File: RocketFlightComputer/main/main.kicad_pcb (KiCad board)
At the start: 2 copper layers, 62 x 62 mm, 0 parts

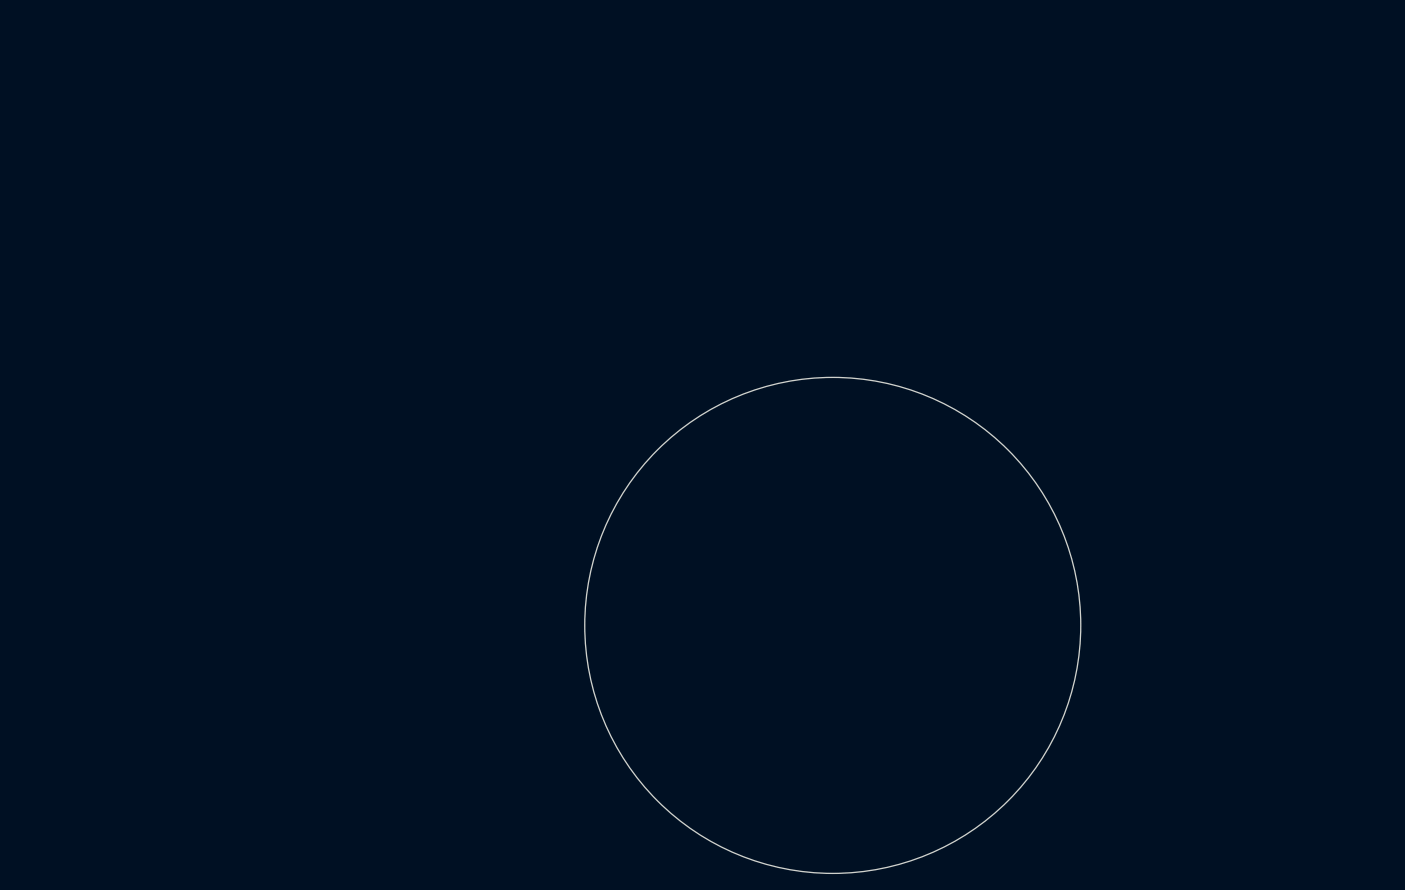
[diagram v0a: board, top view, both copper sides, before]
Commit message: CID documentation and started the PCB editor process
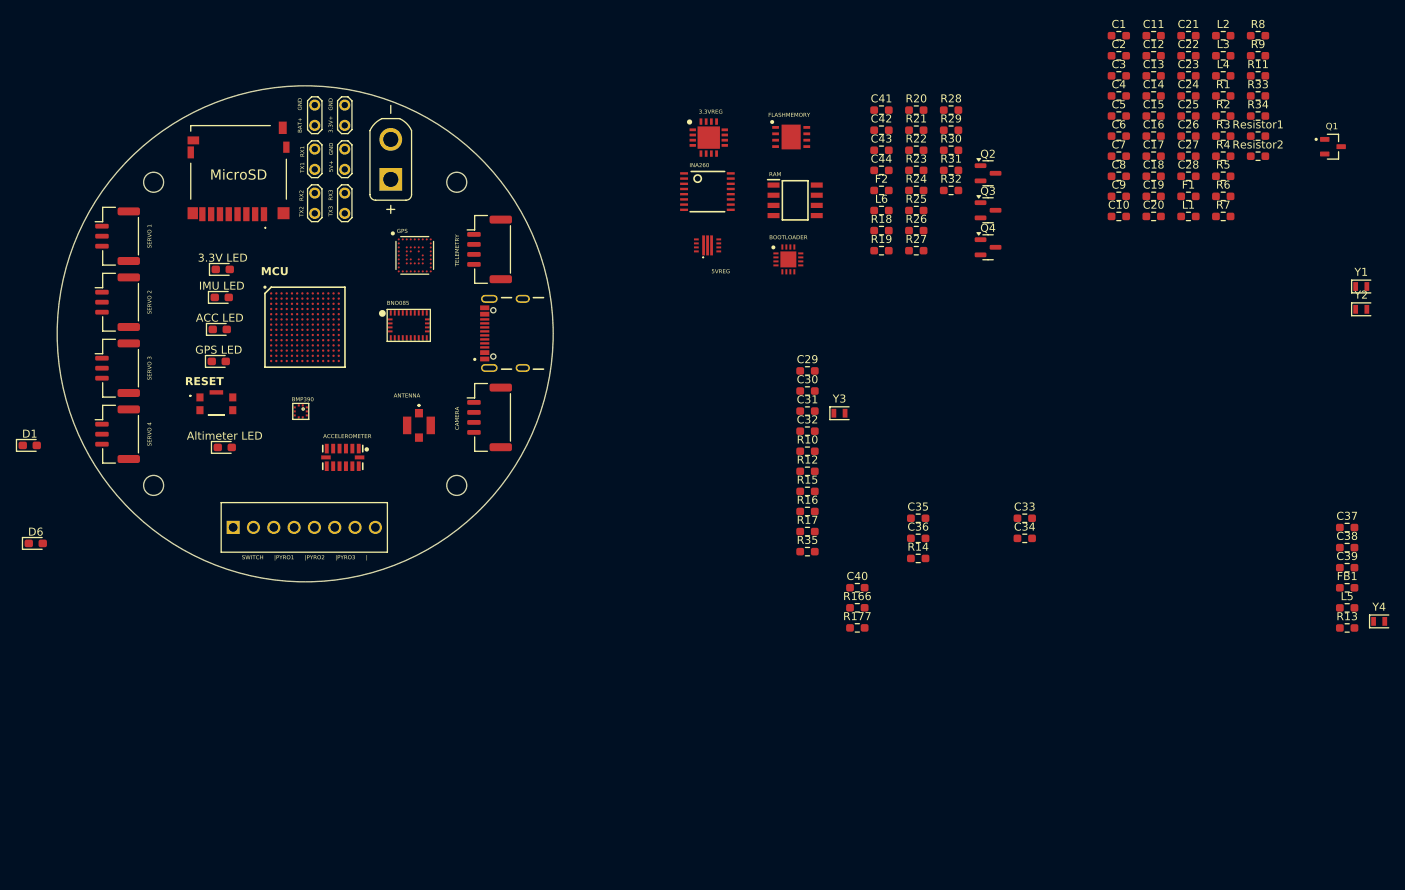
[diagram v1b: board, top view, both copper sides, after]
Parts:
- added 3.3V LED: 3.3V LED, LED_SMD:LED_0603_1608Metric_Pad1.05x0.95mm_HandSolder, F.Cu at (103.2, 89.2)
- added 3.3V+   GND: TestPoint_2Pole, TestPoint:TestPoint_2Pads_Pitch2.54mm_Drill0.8mm, F.Cu at (118.5, 71.2)
- added 3.3VREG: TPS62111RSAR, footprint:TPS62111RSAR, F.Cu at (164.0, 72.8)
- added 5V+   GND: TestPoint_2Pole, TestPoint:TestPoint_2Pads_Pitch2.54mm_Drill0.8mm, F.Cu at (118.5, 76.8)
- added 5VREG: TPS621361RGXT, footprint:TPS621361RGXT, F.Cu at (163.8, 86.2)
- added ACC LED: 200G ACC LED, LED_SMD:LED_0603_1608Metric_Pad1.05x0.95mm_HandSolder, F.Cu at (102.9, 96.8)
- added ACCELEROMETER: ADXL375, ADXL375:LGA14, F.Cu at (118.2, 112.8)
- added ANTENNA: CONMHF1-SMD-G-T, footprint:CONMHF1SMDGT, F.Cu at (127.8, 108.8)
- added Altimeter LED: Altimeter LED, LED_SMD:LED_0603_1608Metric_Pad1.05x0.95mm_HandSolder, F.Cu at (103.5, 111.5)
- added BAT+    GND: TestPoint_2Pole, TestPoint:TestPoint_2Pads_Pitch2.54mm_Drill0.8mm, F.Cu at (114.8, 71.2)
- added BMP390: BMP390, BMP390:BMP388, F.Cu at (113.0, 107.0)
- added BOOTLOADER: MKL02Z32VFG4, footprint:QFN50P300X300X65-17N-D, F.Cu at (173.9, 88.0)
- added BatteryConnector1: XT30UPB-M, XT30:AMASS_XT30UPB-M, F.Cu at (124.2, 75.5)
- added C1: 10uF, Resistor_SMD:R_0603_1608Metric_Pad0.98x0.95mm_HandSolder, F.Cu at (215.3, 60.0)
- added C10: 20pF, Resistor_SMD:R_0603_1608Metric_Pad0.98x0.95mm_HandSolder, F.Cu at (215.3, 82.6)
- added C11: 20pF, Resistor_SMD:R_0603_1608Metric_Pad0.98x0.95mm_HandSolder, F.Cu at (219.6, 60.0)
- added C12: 10uF, Resistor_SMD:R_0603_1608Metric_Pad0.98x0.95mm_HandSolder, F.Cu at (219.6, 62.5)
- added C13: 0.22uF, Resistor_SMD:R_0603_1608Metric_Pad0.98x0.95mm_HandSolder, F.Cu at (219.6, 65.1)
- added C14: 0.22uF, Resistor_SMD:R_0603_1608Metric_Pad0.98x0.95mm_HandSolder, F.Cu at (219.6, 67.6)
- added C15: 4.7uF, Resistor_SMD:R_0603_1608Metric_Pad0.98x0.95mm_HandSolder, F.Cu at (219.6, 70.1)
- added C16: 4.7uF, Resistor_SMD:R_0603_1608Metric_Pad0.98x0.95mm_HandSolder, F.Cu at (219.6, 72.6)
- added C17: 4.7uF, Resistor_SMD:R_0603_1608Metric_Pad0.98x0.95mm_HandSolder, F.Cu at (219.6, 75.1)
- added C18: 0.22uF, Resistor_SMD:R_0603_1608Metric_Pad0.98x0.95mm_HandSolder, F.Cu at (219.6, 77.6)
- added C19: 0.22uF, Resistor_SMD:R_0603_1608Metric_Pad0.98x0.95mm_HandSolder, F.Cu at (219.6, 80.1)
- added C2: 22uF, Resistor_SMD:R_0603_1608Metric_Pad0.98x0.95mm_HandSolder, F.Cu at (215.3, 62.5)
- added C20: 0.22uF, Resistor_SMD:R_0603_1608Metric_Pad0.98x0.95mm_HandSolder, F.Cu at (219.6, 82.6)
- added C21: 0.22uF, Resistor_SMD:R_0603_1608Metric_Pad0.98x0.95mm_HandSolder, F.Cu at (224.0, 60.0)
- added C22: 0.22uF, Resistor_SMD:R_0603_1608Metric_Pad0.98x0.95mm_HandSolder, F.Cu at (224.0, 62.5)
- added C23: 12pF, Resistor_SMD:R_0603_1608Metric_Pad0.98x0.95mm_HandSolder, F.Cu at (224.0, 65.1)
- added C24: 12pF, Resistor_SMD:R_0603_1608Metric_Pad0.98x0.95mm_HandSolder, F.Cu at (224.0, 67.6)
- added C25: 10nF, Resistor_SMD:R_0603_1608Metric_Pad0.98x0.95mm_HandSolder, F.Cu at (224.0, 70.1)
- added C26: 0.22uF, Resistor_SMD:R_0603_1608Metric_Pad0.98x0.95mm_HandSolder, F.Cu at (224.0, 72.6)
- added C27: 4.7uF, Resistor_SMD:R_0603_1608Metric_Pad0.98x0.95mm_HandSolder, F.Cu at (224.0, 75.1)
- added C28: 10uF, Resistor_SMD:R_0603_1608Metric_Pad0.98x0.95mm_HandSolder, F.Cu at (224.0, 77.6)
- added C29: 0.1uF, Resistor_SMD:R_0603_1608Metric_Pad0.98x0.95mm_HandSolder, F.Cu at (176.3, 101.9)
- added C3: 1uF, Resistor_SMD:R_0603_1608Metric_Pad0.98x0.95mm_HandSolder, F.Cu at (215.3, 65.1)
- added C30: 0.1uF, Resistor_SMD:R_0603_1608Metric_Pad0.98x0.95mm_HandSolder, F.Cu at (176.3, 104.5)
- added C31: 22pF, Resistor_SMD:R_0603_1608Metric_Pad0.98x0.95mm_HandSolder, F.Cu at (176.3, 107.0)
- added C32: 22pF, Resistor_SMD:R_0603_1608Metric_Pad0.98x0.95mm_HandSolder, F.Cu at (176.3, 109.5)
- added C33: 0.1uF, Resistor_SMD:R_0603_1608Metric_Pad0.98x0.95mm_HandSolder, F.Cu at (203.5, 120.4)
- added C34: 0.1uF, Resistor_SMD:R_0603_1608Metric_Pad0.98x0.95mm_HandSolder, F.Cu at (203.5, 122.9)
- added C35: 1uF, Resistor_SMD:R_0603_1608Metric_Pad0.98x0.95mm_HandSolder, F.Cu at (190.2, 120.4)
- added C36: 0.1uF, Resistor_SMD:R_0603_1608Metric_Pad0.98x0.95mm_HandSolder, F.Cu at (190.2, 122.9)
- added C37: 47PF-0603-50V-5%, Resistor_SMD:R_0603_1608Metric_Pad0.98x0.95mm_HandSolder, F.Cu at (243.8, 121.5)
- added C38: 4.7UF, Resistor_SMD:R_0603_1608Metric_Pad0.98x0.95mm_HandSolder, F.Cu at (243.8, 124.0)
- added C39: 0.1UF, Resistor_SMD:R_0603_1608Metric_Pad0.98x0.95mm_HandSolder, F.Cu at (243.8, 126.5)
- added C4: 0.22uF, Resistor_SMD:R_0603_1608Metric_Pad0.98x0.95mm_HandSolder, F.Cu at (215.3, 67.6)
- added C40: 1uF, Resistor_SMD:R_0603_1608Metric_Pad0.98x0.95mm_HandSolder, F.Cu at (182.6, 129.0)
- added C41: 10uF, Resistor_SMD:R_0603_1608Metric_Pad0.98x0.95mm_HandSolder, F.Cu at (185.6, 69.3)
- added C42: 22uF, Resistor_SMD:R_0603_1608Metric_Pad0.98x0.95mm_HandSolder, F.Cu at (185.6, 71.8)
- added C43: 22uF, Resistor_SMD:R_0603_1608Metric_Pad0.98x0.95mm_HandSolder, F.Cu at (185.6, 74.4)
- added C44: 3.3nF, Resistor_SMD:R_0603_1608Metric_Pad0.98x0.95mm_HandSolder, F.Cu at (185.6, 76.9)
- added C5: 0.22uF, Resistor_SMD:R_0603_1608Metric_Pad0.98x0.95mm_HandSolder, F.Cu at (215.3, 70.1)
- added C6: 0.22uF, Resistor_SMD:R_0603_1608Metric_Pad0.98x0.95mm_HandSolder, F.Cu at (215.3, 72.6)
- added C7: 2.2uF, Resistor_SMD:R_0603_1608Metric_Pad0.98x0.95mm_HandSolder, F.Cu at (215.3, 75.1)
- added C8: 10nF, Resistor_SMD:R_0603_1608Metric_Pad0.98x0.95mm_HandSolder, F.Cu at (215.3, 77.6)
- added C9: 4.7uF, Resistor_SMD:R_0603_1608Metric_Pad0.98x0.95mm_HandSolder, F.Cu at (215.3, 80.1)
- added CAMERA: S4B-PH-K-S_LF__SN_, Connector_JST:JST_GH_BM04B-GHS-TBT_1x04-1MP_P1.25mm_Vertical, F.Cu at (136.6, 107.8)
- added D1: LED, LED_SMD:LED_0603_1608Metric_Pad1.05x0.95mm_HandSolder, F.Cu at (79.1, 111.2)
- added D6: Misc LED, LED_SMD:LED_0603_1608Metric_Pad1.05x0.95mm_HandSolder, F.Cu at (79.9, 123.5)
- added F1: 1A, Resistor_SMD:R_0603_1608Metric_Pad0.98x0.95mm_HandSolder, F.Cu at (224.0, 80.1)
- added F2: 5A, Resistor_SMD:R_0603_1608Metric_Pad0.98x0.95mm_HandSolder, F.Cu at (185.6, 79.4)
- added FB1: 120ohm, Resistor_SMD:R_0603_1608Metric_Pad0.98x0.95mm_HandSolder, F.Cu at (243.8, 129.1)
- added FLASHMEMORY: W25Q64JVXGIM_TR, footprint:SON80P400X400X50-9N, F.Cu at (174.3, 72.7)
- added GPS LED: GPS LED, LED_SMD:LED_0603_1608Metric_Pad1.05x0.95mm_HandSolder, F.Cu at (102.8, 100.8)
- added IMU LED: IMU LED, LED_SMD:LED_0603_1608Metric_Pad1.05x0.95mm_HandSolder, F.Cu at (103.1, 92.8)
- added INA260: INA260, INA260:TSSOP16, F.Cu at (163.8, 79.5)
- added L1: 120, Resistor_SMD:R_0603_1608Metric_Pad0.98x0.95mm_HandSolder, F.Cu at (224.0, 82.6)
- added L2: 6.8uH, Resistor_SMD:R_0603_1608Metric_Pad0.98x0.95mm_HandSolder, F.Cu at (228.3, 60.0)
- added L3: 120, Resistor_SMD:R_0603_1608Metric_Pad0.98x0.95mm_HandSolder, F.Cu at (228.3, 62.5)
- added L4: 4.7uH, Resistor_SMD:R_0603_1608Metric_Pad0.98x0.95mm_HandSolder, F.Cu at (228.3, 65.1)
- added L5: 2.2μ, Resistor_SMD:R_0603_1608Metric_Pad0.98x0.95mm_HandSolder, F.Cu at (243.8, 131.6)
- added L6: 1.5uH, Resistor_SMD:R_0603_1608Metric_Pad0.98x0.95mm_HandSolder, F.Cu at (185.6, 81.9)
- added MCU: MIMXRT1062DVL6B, footprint:BGA196C65P14X14_1000X1000X152, F.Cu at (113.5, 96.5)
- added MicroSD: DM3D-SF, DM3DSF:DM3DSF, F.Cu at (105.2, 77.0)
- added Q1: DMG2305UX, footprint:DMG2305UX, F.Cu at (242.0, 73.9)
- added Q2: SI2302, Package_TO_SOT_SMD:SOT-23, F.Cu at (198.9, 77.2)
- added Q3: SI2302, Package_TO_SOT_SMD:SOT-23, F.Cu at (198.9, 81.9)
- added Q4: SI2302, Package_TO_SOT_SMD:SOT-23, F.Cu at (198.9, 86.5)
- added R1: 1M, Resistor_SMD:R_0603_1608Metric_Pad0.98x0.95mm_HandSolder, F.Cu at (228.3, 67.6)
- added R10: 10k, Resistor_SMD:R_0603_1608Metric_Pad0.98x0.95mm_HandSolder, F.Cu at (176.3, 112.0)
- added R11: 4.7k, Resistor_SMD:R_0603_1608Metric_Pad0.98x0.95mm_HandSolder, F.Cu at (232.7, 65.1)
- added R12: 10k, Resistor_SMD:R_0603_1608Metric_Pad0.98x0.95mm_HandSolder, F.Cu at (176.3, 114.5)
- added R13: 10OHM-0603-1/10W-1%, Resistor_SMD:R_0603_1608Metric_Pad0.98x0.95mm_HandSolder, F.Cu at (243.8, 134.1)
- added R14: 10k, Resistor_SMD:R_0603_1608Metric_Pad0.98x0.95mm_HandSolder, F.Cu at (190.2, 125.4)
- added R15: 4.7k, Resistor_SMD:R_0603_1608Metric_Pad0.98x0.95mm_HandSolder, F.Cu at (176.3, 117.0)
- added R16: 4.7k, Resistor_SMD:R_0603_1608Metric_Pad0.98x0.95mm_HandSolder, F.Cu at (176.3, 119.5)
- added R166: 10K, Resistor_SMD:R_0603_1608Metric_Pad0.98x0.95mm_HandSolder, F.Cu at (182.6, 131.6)
- added R17: 4.7k, Resistor_SMD:R_0603_1608Metric_Pad0.98x0.95mm_HandSolder, F.Cu at (176.3, 122.0)
- added R177: 10K, Resistor_SMD:R_0603_1608Metric_Pad0.98x0.95mm_HandSolder, F.Cu at (182.6, 134.1)
- added R18: 10k, Resistor_SMD:R_0603_1608Metric_Pad0.98x0.95mm_HandSolder, F.Cu at (185.6, 84.4)
- added R19: 4, Resistor_SMD:R_0603_1608Metric_Pad0.98x0.95mm_HandSolder, F.Cu at (185.6, 86.9)
- added R2: 470, Resistor_SMD:R_0603_1608Metric_Pad0.98x0.95mm_HandSolder, F.Cu at (228.3, 70.1)
- added R20: 7k, Resistor_SMD:R_0603_1608Metric_Pad0.98x0.95mm_HandSolder, F.Cu at (189.9, 69.3)
- added R21: 10k, Resistor_SMD:R_0603_1608Metric_Pad0.98x0.95mm_HandSolder, F.Cu at (189.9, 71.8)
- added R22: 470k, Resistor_SMD:R_0603_1608Metric_Pad0.98x0.95mm_HandSolder, F.Cu at (189.9, 74.4)
- added R23: 10k, Resistor_SMD:R_0603_1608Metric_Pad0.98x0.95mm_HandSolder, F.Cu at (189.9, 76.9)
- added R24: 4, Resistor_SMD:R_0603_1608Metric_Pad0.98x0.95mm_HandSolder, F.Cu at (189.9, 79.4)
- added R25: 510k, Resistor_SMD:R_0603_1608Metric_Pad0.98x0.95mm_HandSolder, F.Cu at (189.9, 81.9)
- added R26: 82k, Resistor_SMD:R_0603_1608Metric_Pad0.98x0.95mm_HandSolder, F.Cu at (189.9, 84.4)
- added R27: 7k, Resistor_SMD:R_0603_1608Metric_Pad0.98x0.95mm_HandSolder, F.Cu at (189.9, 86.9)
- added R28: 10k, Resistor_SMD:R_0603_1608Metric_Pad0.98x0.95mm_HandSolder, F.Cu at (194.3, 69.3)
- added R29: 10k, Resistor_SMD:R_0603_1608Metric_Pad0.98x0.95mm_HandSolder, F.Cu at (194.3, 71.8)
- added R3: 470, Resistor_SMD:R_0603_1608Metric_Pad0.98x0.95mm_HandSolder, F.Cu at (228.3, 72.6)
- added R30: 4, Resistor_SMD:R_0603_1608Metric_Pad0.98x0.95mm_HandSolder, F.Cu at (194.3, 74.4)
- added R31: 7k, Resistor_SMD:R_0603_1608Metric_Pad0.98x0.95mm_HandSolder, F.Cu at (194.3, 76.9)
- added R32: 10k, Resistor_SMD:R_0603_1608Metric_Pad0.98x0.95mm_HandSolder, F.Cu at (194.3, 79.4)
- added R33: 470, Resistor_SMD:R_0603_1608Metric_Pad0.98x0.95mm_HandSolder, F.Cu at (232.7, 67.6)
- added R34: 4.7k, Resistor_SMD:R_0603_1608Metric_Pad0.98x0.95mm_HandSolder, F.Cu at (232.7, 70.1)
- added R35: 10k, Resistor_SMD:R_0603_1608Metric_Pad0.98x0.95mm_HandSolder, F.Cu at (176.3, 124.5)
- added R4: 2.2M, Resistor_SMD:R_0603_1608Metric_Pad0.98x0.95mm_HandSolder, F.Cu at (228.3, 75.1)
- added R5: 470, Resistor_SMD:R_0603_1608Metric_Pad0.98x0.95mm_HandSolder, F.Cu at (228.3, 77.6)
- added R6: 470, Resistor_SMD:R_0603_1608Metric_Pad0.98x0.95mm_HandSolder, F.Cu at (228.3, 80.1)
- added R7: 470, Resistor_SMD:R_0603_1608Metric_Pad0.98x0.95mm_HandSolder, F.Cu at (228.3, 82.6)
- added R8: 470, Resistor_SMD:R_0603_1608Metric_Pad0.98x0.95mm_HandSolder, F.Cu at (232.7, 60.0)
- added R9: 100k, Resistor_SMD:R_0603_1608Metric_Pad0.98x0.95mm_HandSolder, F.Cu at (232.7, 62.5)
- added RAM: APS6404L-3SQR-SN, footprint:APS6404L, F.Cu at (174.8, 80.6)
- added REF**: MountingHole_2.5mm, MountingHole:MountingHole_2.5mm, F.Cu at (94.6, 116.2)
- added REF**: MountingHole_2.5mm, MountingHole:MountingHole_2.5mm, F.Cu at (132.5, 116.2)
- added REF**: MountingHole_2.5mm, MountingHole:MountingHole_2.5mm, F.Cu at (132.5, 78.4)
- added REF**: MountingHole_2.5mm, MountingHole:MountingHole_2.5mm, F.Cu at (94.6, 78.4)
- added RESET: KMR241GLFS, footprint:KMR421GULCLFS, F.Cu at (102.5, 106.0)
- added Resistor1: 5.1k, Resistor_SMD:R_0603_1608Metric_Pad0.98x0.95mm_HandSolder, F.Cu at (232.7, 72.6)
- added Resistor2: 5.1k, Resistor_SMD:R_0603_1608Metric_Pad0.98x0.95mm_HandSolder, F.Cu at (232.7, 75.1)
- added SERVO 1: ~, Connector_JST:JST_GH_BM03B-GHS-TBT_1x03-1MP_P1.25mm_Vertical, F.Cu at (90.1, 85.1)
- added SERVO 2: ~, Connector_JST:JST_GH_BM03B-GHS-TBT_1x03-1MP_P1.25mm_Vertical, F.Cu at (90.1, 93.3)
- added SERVO 3: ~, Connector_JST:JST_GH_BM03B-GHS-TBT_1x03-1MP_P1.25mm_Vertical, F.Cu at (90.1, 101.6)
- added SERVO 4: ~, Connector_JST:JST_GH_BM03B-GHS-TBT_1x03-1MP_P1.25mm_Vertical, F.Cu at (90.1, 109.8)
- added SWITCH      |PYRO1      |PYRO2      |PYRO3      |: 1725711, footprint:1725711, F.Cu at (104.5, 121.5)
- added TELEMETRY: S4B-PH-K-S_LF__SN_, Connector_JST:JST_GH_BM04B-GHS-TBT_1x04-1MP_P1.25mm_Vertical, F.Cu at (136.6, 86.8)
- added TX1   RX1: TestPoint_2Pole, TestPoint:TestPoint_2Pads_Pitch2.54mm_Drill0.8mm, F.Cu at (114.8, 76.8)
- added TX2   RX2: TestPoint_2Pole, TestPoint:TestPoint_2Pads_Pitch2.54mm_Drill0.8mm, F.Cu at (114.8, 82.2)
- added TX3   RX3: TestPoint_2Pole, TestPoint:TestPoint_2Pads_Pitch2.54mm_Drill0.8mm, F.Cu at (118.5, 82.2)
- added U1: BNO085, BNO08x:BNO080, F.Cu at (126.5, 96.2)
- added U3: GPS, ZOE-M8Q:UBLOX_ZOE_M8-0-10, F.Cu at (127.2, 87.5)
- added USBc1: USBc, footprint:GCT_USB4105-GF-A, F.Cu at (140.8, 97.2)
- added Y1: 32.768kHz, Crystal:Crystal_SMD_2012-2Pin_2.0x1.2mm, F.Cu at (245.6, 91.4)
- added Y2: 24MHz, Crystal:Crystal_SMD_2012-2Pin_2.0x1.2mm, F.Cu at (245.6, 94.2)
- added Y3: 32.768kHz, Crystal:Crystal_SMD_2012-2Pin_2.0x1.2mm, F.Cu at (180.3, 107.2)
- added Y4: 32.768kHz, Crystal:Crystal_SMD_2012-2Pin_2.0x1.2mm, F.Cu at (247.8, 133.2)
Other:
- copper layers 2 -> 4

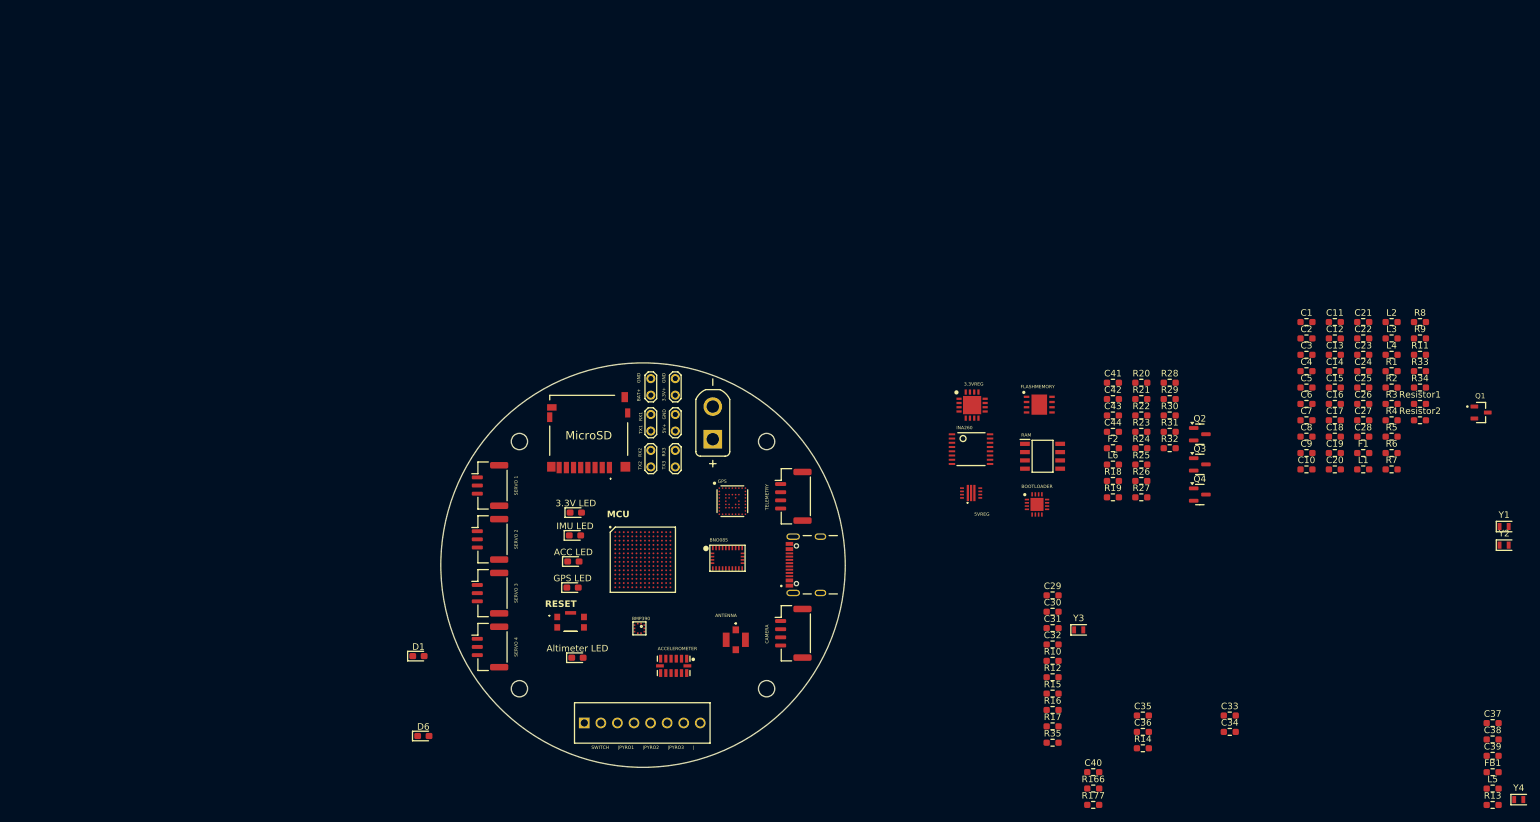
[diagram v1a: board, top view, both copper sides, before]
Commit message: Layout of PCB mostly done
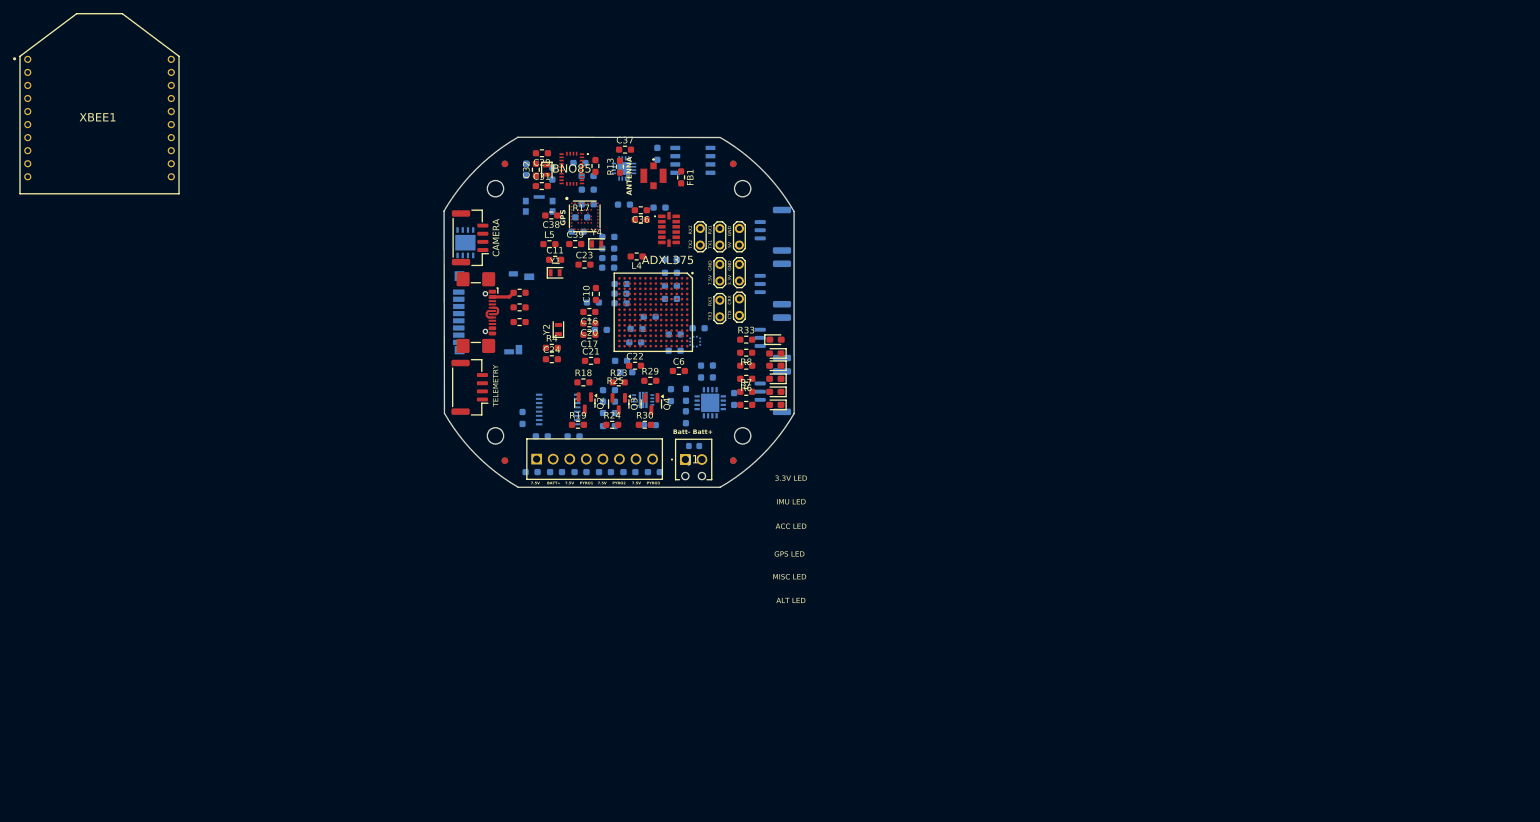
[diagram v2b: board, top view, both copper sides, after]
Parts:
- removed ACCELEROMETER: ADXL375, ADXL375:LGA14
- removed BatteryConnector1: XT30UPB-M, XT30:AMASS_XT30UPB-M
- removed F1: 1A, Resistor_SMD:R_0603_1608Metric_Pad0.98x0.95mm_HandSolder
- removed Q1: DMG2305UX, footprint:DMG2305UX
- removed Resistor1, Resistor2: 5.1k, Resistor_SMD:R_0603_1608Metric_Pad0.98x0.95mm_HandSolder
- removed U1: BNO085, BNO08x:BNO080
- removed USBc1: USBc, footprint:GCT_USB4105-GF-A
- added ADXL375: ACC, footprint:ADXL375BCCZRL, F.Cu at (117.5, 45.8)
- added BNO85: IMU, footprint:BNO085, F.Cu at (102.6, 36.5)
- added FID1: Fiducial, Fiducial:Fiducial_1mm_Mask2mm, F.Cu at (92.4, 35.8)
- added FID2: Fiducial, Fiducial:Fiducial_1mm_Mask2mm, F.Cu at (92.4, 81.3)
- added FID3: Fiducial, Fiducial:Fiducial_1mm_Mask2mm, F.Cu at (127.4, 35.8)
- added FID4: Fiducial, Fiducial:Fiducial_1mm_Mask2mm, B.Cu at (92.4, 35.8)
- added FID5: Fiducial, Fiducial:Fiducial_1mm_Mask2mm, B.Cu at (127.4, 81.3)
- added FID6: Fiducial, Fiducial:Fiducial_1mm_Mask2mm, B.Cu at (92.4, 81.3)
- added FID7: Fiducial, Fiducial:Fiducial_1mm_Mask2mm, B.Cu at (127.4, 35.8)
- added FID8: Fiducial, Fiducial:Fiducial_1mm_Mask2mm, F.Cu at (127.4, 81.3)
- added J1: BATT, footprint:1725656, F.Cu at (120.0, 81.1)
- added Resistor3: 5.1k, Resistor_SMD:R_0603_1608Metric_Pad0.98x0.95mm_HandSolder, F.Cu at (94.6, 57.8)
- added Resistor4: 5.1k, Resistor_SMD:R_0603_1608Metric_Pad0.98x0.95mm_HandSolder, F.Cu at (94.6, 60.0)
- added TP7: TestPoint_2Pole, TestPoint:TestPoint_2Pads_Pitch2.54mm_Drill0.8mm, F.Cu at (128.3, 59.0)
- added USB_C_Receptacle_USB2.0_14P1: USBc, Connector_USB:USB_C_Receptacle_GCT_USB4110, F.Cu at (86.8, 58.6)
- added XBEE1: XB24CAPIT-001, footprint:XB24CAPIT-001, F.Cu at (30.2, 12.8)
- 878-APS6404L-3SQR-SN1: renamed from RAM; value APS6404L-3SQR-SN -> PSRAM; moved to B.Cu
- BMP390: value BMP390 -> ALTIMETER; moved to B.Cu
- C1, C12, C13, C14, C15, C18, C19, C2, C25, C26, C27, C28, C3, C33, C34, C4, C40, C41, C42, C43, C44, C5, C7, C8, C9, INA260, L2, L3, L6, R1, R10, R11, R12, R14, R15, R16, R166, R17, R177, R2, R20, R21, R22, R25, R26, R27, R28, R31, R32, R34, R35, R9: moved to B.Cu
- CONMHF1-SMD-G-T1: renamed from ANTENNA; value CONMHF1-SMD-G-T -> ANTENNA
- D1: value LED -> BOOT LED; moved to B.Cu
- D2: renamed from IMU LED
- D3: renamed from ACC LED
- D4: renamed from Altimeter LED
- D5: renamed from GPS LED
- D8: renamed from 3.3V LED
- DM3D-SF1: renamed from MicroSD; value DM3D-SF -> MicroSD; moved to B.Cu
- F2: footprint Resistor_SMD:R_0603_1608Metric_Pad0.98x0.95mm_HandSolder -> Fuse:Fuse_0603_1608Metric; moved to B.Cu
- KMR241GLFS1: renamed from RESET; value KMR241GLFS -> RESET; moved to B.Cu
- MIMXRT1062DVL6B1: renamed from MCU; value MIMXRT1062DVL6B -> MCU; footprint footprint:BGA196C65P14X14_1000X1000X152 -> footprint:BGA196C80P14X14_1200X1200X152
- MKL02Z32VFG4: renamed from BOOTLOADER; value MKL02Z32VFG4 -> BOOT; moved to B.Cu
- S4B-PH-K-S_LF__SN_1: renamed from TELEMETRY; value S4B-PH-K-S_LF__SN_ -> TELEMETRY
- S4B-PH-K-S_LF__SN_2: renamed from CAMERA; value S4B-PH-K-S_LF__SN_ -> CAMERA
- SERVO1: renamed from SERVO 1; value ~ -> SERVO1; moved to B.Cu
- SERVO2: renamed from SERVO 2; value ~ -> SERVO2; moved to B.Cu
- SERVO3: renamed from SERVO 3; value ~ -> SERVO3; moved to B.Cu
- SERVO4: renamed from SERVO 4; value ~ -> SERVO4; moved to B.Cu
- ScrewTerminal1: renamed from SWITCH      |PYRO1      |PYRO2      |PYRO3      |
- TP1: renamed from 3.3V+   GND
- TP2: renamed from BAT+    GND
- TP3: renamed from 5V+   GND
- TP4: renamed from TX1   RX1
- TP5: renamed from TX2   RX2
- TP6: renamed from TX3   RX3
- TPS62111RSAR1: renamed from 3.3VREG; value TPS62111RSAR -> 3.3Vreg; moved to B.Cu
- TPS621361RGXT1: renamed from 5VREG; value TPS621361RGXT -> 5Vreg; moved to B.Cu
- W25Q64JVXGIM_TR1: renamed from FLASHMEMORY; value W25Q64JVXGIM_TR -> FLASH; moved to B.Cu
- moved L5 167.0 mm to (99.2, 48.1)
- moved R13 165.7 mm to (110.0, 36.2), turned to 90 degrees
- moved C38 165.2 mm to (99.5, 43.7), turned to 180 degrees
- moved Y4 165.0 mm to (106.4, 48.1)
- moved C39 161.0 mm to (103.2, 48.1)
- moved C37 159.4 mm to (110.8, 33.6)
- moved FB1 154.2 mm to (119.4, 37.9), turned to -90 degrees
- moved Y1 150.6 mm to (100.1, 52.5)
- moved Y2 148.7 mm to (100.6, 61.2), turned to 90 degrees
- moved R2 132.8 mm to (99.7, 37.3), turned to -90 degrees
- moved L1 132.1 mm to (94.6, 55.5)
- moved R4 129.2 mm to (99.6, 64.0)
- moved R9 125.6 mm to (107.1, 61.2), turned to 180 degrees
- moved C24 124.4 mm to (99.6, 65.7)
- moved L3 121.1 mm to (108.2, 47.0), turned to 180 degrees
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- renumbered U3 to U-BLOX_ZOE_M8Q-0-10
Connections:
- C13 pad 1: +3.3V -> Net-(MIMXRT1062DVL6B1-VDD_USB_CAP)
- C8 pad 1: +3.3V -> Net-(MIMXRT1062DVL6B1-VDD_USB_CAP)
- L1 pad 2: Net-(L1-Pad2) -> Net-(MIMXRT1062DVL6B1-USB_OTG1_VBUS)
- MIMXRT1062DVL6B1 pad F10: unconnected-(MCU1-NVCC_GPIO_2-PadF10) -> +3.3V
- MIMXRT1062DVL6B1 pad H13: unconnected-(MCU1-GPIO_AD_B1_08-PadH13) -> /Reserve_CTX
- MIMXRT1062DVL6B1 pad H9: unconnected-(MCU1-VDD_SOC_IN_8-PadH9) -> /M1M2
- MIMXRT1062DVL6B1 pad K8: +3.3V -> Net-(MIMXRT1062DVL6B1-VDD_USB_CAP)
- MIMXRT1062DVL6B1 pad M13: unconnected-(MCU1-GPIO_AD_B1_09-PadM13) -> /Reserve_CRX
- MIMXRT1062DVL6B1 pad N1: unconnected-(MCU1-DCDC_GND_1-PadN1) -> GNDREF
- MIMXRT1062DVL6B1 pad N14: /3.3V -> +3.3V
- MIMXRT1062DVL6B1 pad N2: unconnected-(MCU1-DCDC_GND_2-PadN2) -> GNDREF
- MIMXRT1062DVL6B1 pad N6: +7.5V -> Net-(MIMXRT1062DVL6B1-USB_OTG1_VBUS)
- MIMXRT1062DVL6B1 pad P12: /3.3V -> +3.3V
- MIMXRT1062DVL6B1 pad P6: +7.5V -> unconnected-(MIMXRT1062DVL6B1-USB_OTG2_VBUS-PadP6)
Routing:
- net Net-(L1-Pad1): track 0.00 -> 3.52 mm
- net /D-: track 0.00 -> 2.44 mm
- net /D+: track 0.00 -> 2.44 mm
- added copper zone on In1.Cu, net GNDREF
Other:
- board size 62 x 62 mm -> 53.7 x 53.7 mm
- board text added: "3.3V GND"
- board text added: "3.3V LED"
- board text added: "5V GND"
- board text added: "7.5V"
- board text added: "7.5V GND"
- board text added: "ACC LED"
- board text added: "ALT LED"
- board text added: "BATT+"
- board text added: "Batt- Batt+"
- board text added: "CTX CRX"
- board text added: "GPS LED"
- board text added: "IMU LED"
- board text added: "LED"
- board text added: "MISC LED"
- board text added: "PYRO1"
- board text added: "PYRO2"
- board text added: "PYRO3"
- board text added: "TX1 RX1"
- board text added: "TX2 RX2"
- board text added: "TX3 RX3"
